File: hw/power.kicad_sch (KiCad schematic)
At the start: 26 parts

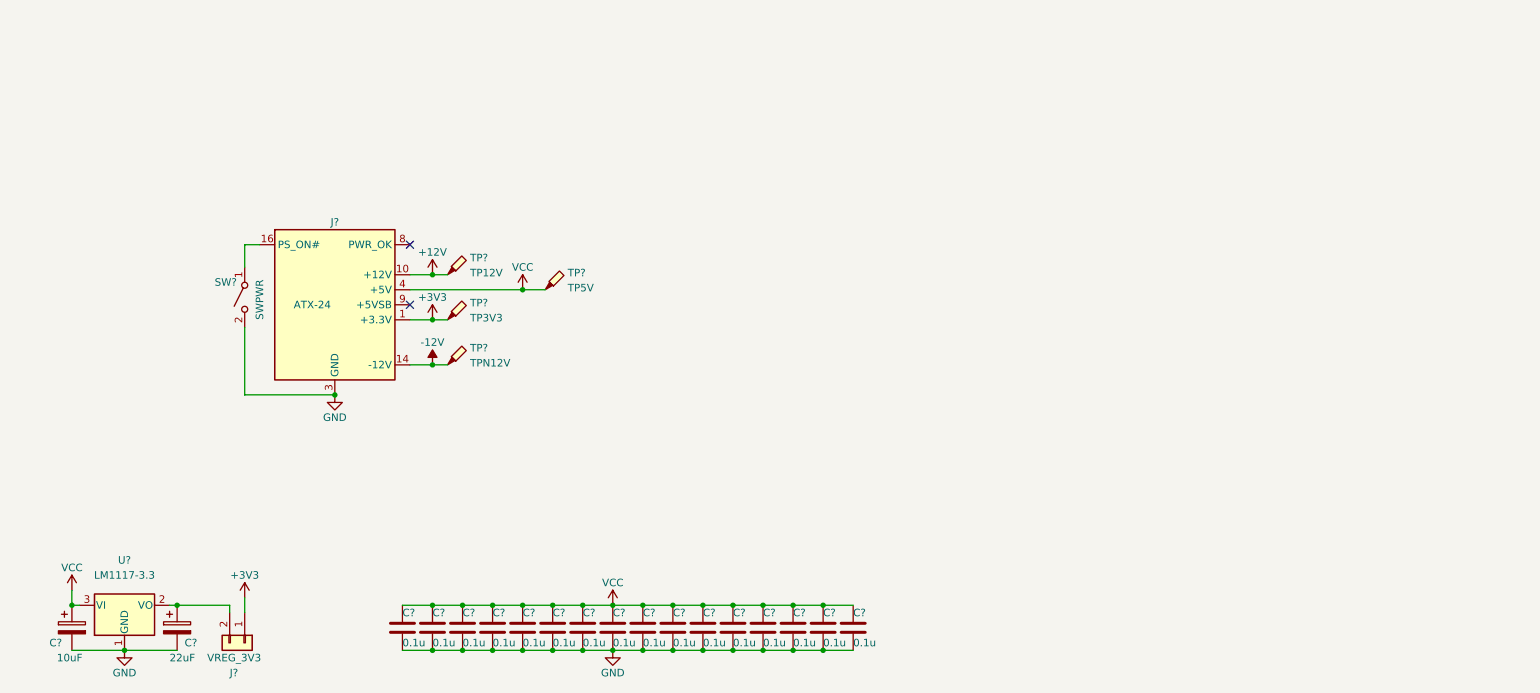
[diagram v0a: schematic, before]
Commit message: decoupling, test points, and ATA0EN/ATA1EN in iodecode.pld
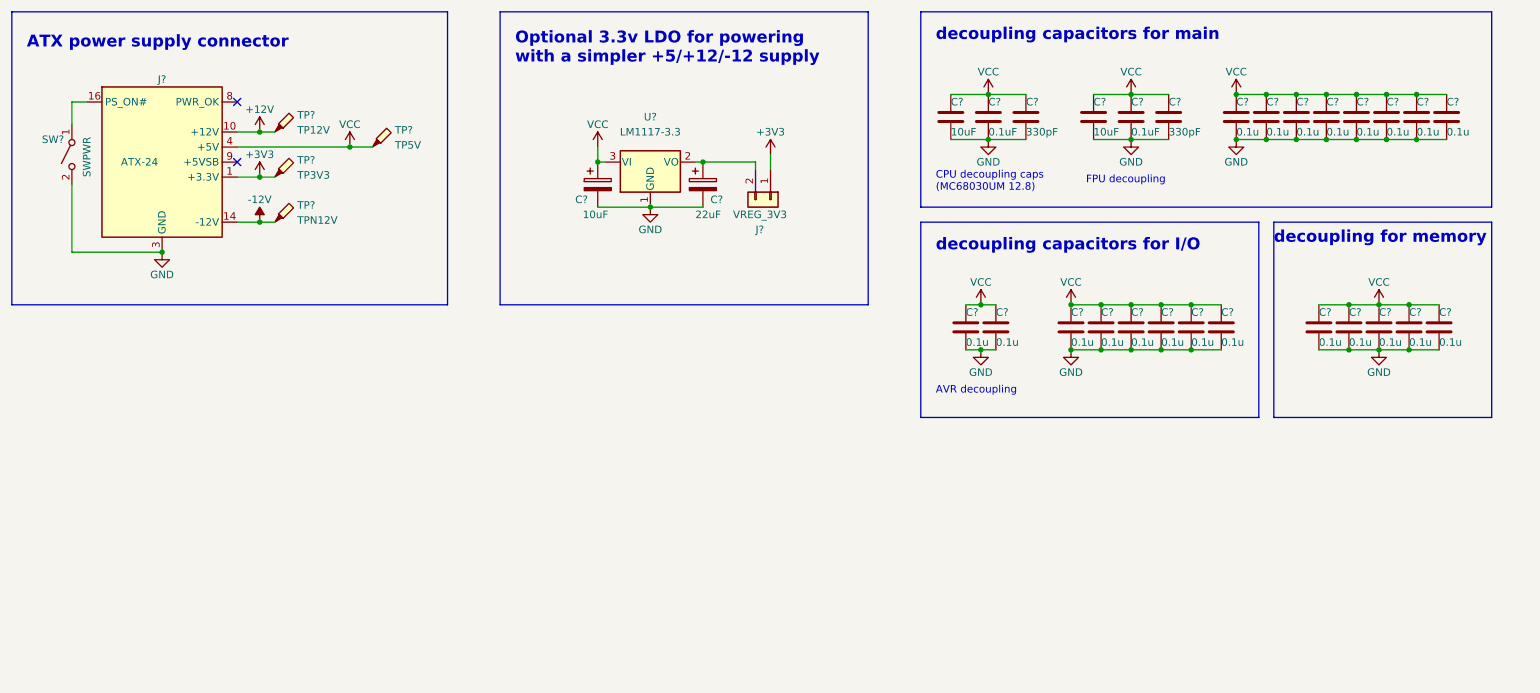
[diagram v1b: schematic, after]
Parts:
- removed C? (x8): 0.1u, symbol Device:C
- added C? (x13): 0.1u, symbol Device:C
- added C? (x2): 10uF, symbol Device:C
- added C? (x2): 330pF, symbol Device:C
- added C? (x2): 0.1uF, symbol Device:C
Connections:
- net GND: now also C?.2, C?.2, C?.2, C?.2, C?.2, C?.2, C?.2, C?.2, C?.2, C?.2, C?.2, C?.2, C?.2, C?.2, C?.2, C?.2, C?.2, C?.2, C?.2
- net VCC: now also C?.1, C?.1, C?.1, C?.1, C?.1, C?.1, C?.1, C?.1, C?.1, C?.1, C?.1, C?.1, C?.1, C?.1, C?.1, C?.1, C?.1, C?.1, C?.1
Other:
- note added: "ATX power supply connector"
- note added: "AVR decoupling"
- note added: "CPU decoupling caps (MC68030UM 12.8)"
- note added: "FPU decoupling"
- note added: "Optional 3.3v LDO for powering with a simpler +5/+12/-12 supply"
- note added: "decoupling capacitors for I/O"
- note added: "decoupling capacitors for main"
- note added: "decoupling for memory"
- title: (none) -> 68030 computer
- moved on the sheet: C?, J?, SW?, TP?, U?

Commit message: fixed ERC errors
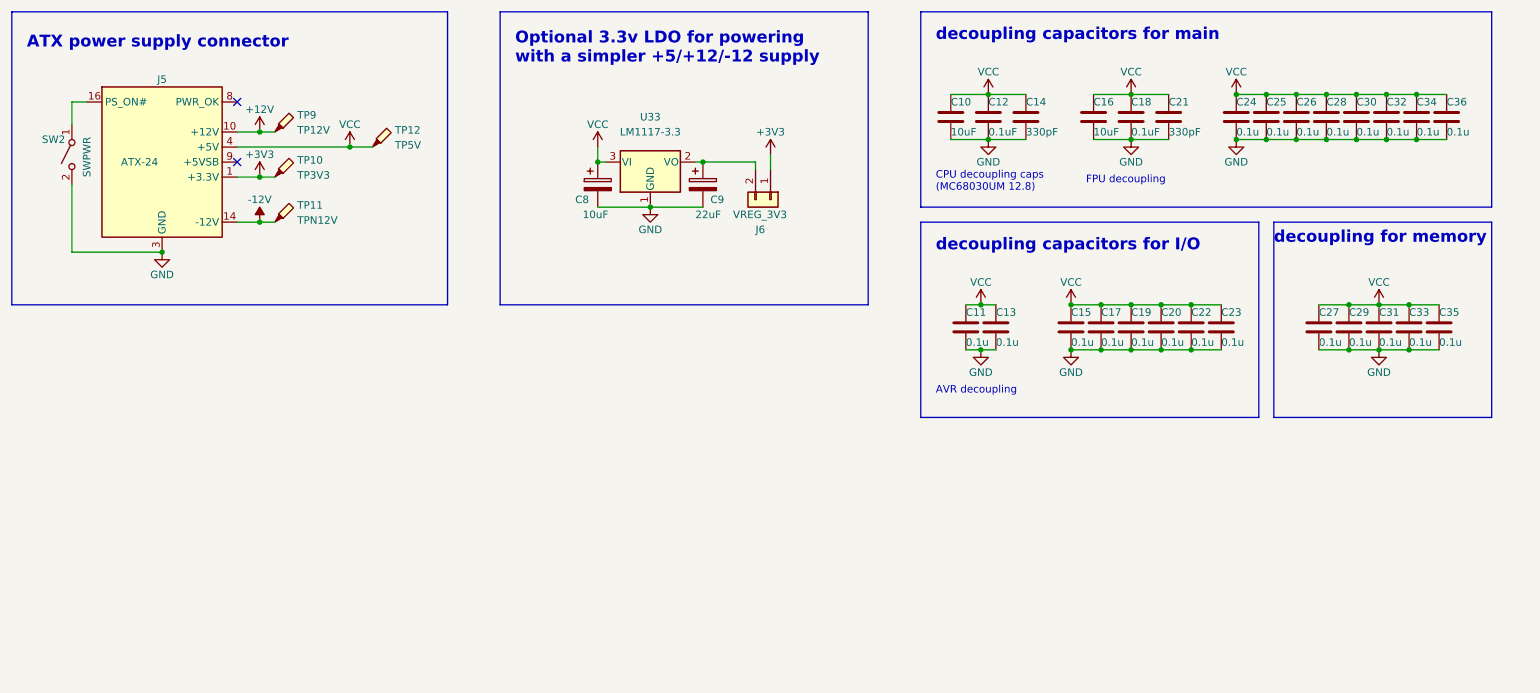
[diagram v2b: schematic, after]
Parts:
- gave numbers to parts that had none: 37

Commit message: first pass at assigning footprints
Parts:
- C10, C11, C12, C13, C14, C15, C16, C17, C18, C19, C20, C21, C22, C23, C24, C25, C26, C27, C28, C29, C30, C31, C32, C33, C34, C35, C36: footprint (none) -> Capacitor_SMD:C_0805_2012Metric_Pad1.18x1.45mm_HandSolder
- J5: footprint (none) -> Connector_Molex:Molex_Mini-Fit_Jr_5566-24A_2x12_P4.20mm_Vertical
- J6, SW2: footprint (none) -> Connector_PinHeader_2.54mm:PinHeader_1x02_P2.54mm_Vertical
- TP10, TP11, TP12, TP9: footprint (none) -> TestPoint:TestPoint_Pad_D1.5mm
- U33: footprint (none) -> Package_TO_SOT_SMD:SOT-223-3_TabPin2

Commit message: finished the footprints
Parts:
- C8, C9: footprint (none) -> Capacitor_SMD:CP_Elec_4x4.5
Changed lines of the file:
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@@
       (effects (font (size 1.27 1.27)) (justify left))
     )
-    (property "Footprint" "" (id 2) (at 143.2052 58.42 0)
+    (property "Footprint" "Capacitor_SMD:CP_Elec_4x4.5" (id 2) (at 143.2052 58.42 0)
       (effects (font (size 1.27 1.27)) hide)
     )
@@
       (effects (font (size 1.27 1.27)) (justify left))
     )
-    (property "Footprint" "" (id 2) (at 125.4252 58.42 0)
-      (effects (font (size 1.27 1.27)) hide)
-    )
+    (property "Footprint" "Capacitor_SMD:CP_Elec_4x4.5" (id 2) (at 125.4252 58.42 0)
+      (effects (font (size 1.27 1.27)) hide)
+    )
